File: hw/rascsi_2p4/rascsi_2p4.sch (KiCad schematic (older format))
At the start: 89 parts, among them J1 Raspberry_Pi_2_3, J2 DNP, J4 I2C Pinout, J5 DNP, J6 CONNFLY DB-25, J7 DNP, U1 74ALVC164245DGG, U2 74ALVC164245DGG, U3 UCC5606PWPTR, U4 UCC5606PWPTR, X1 Mac, X3 Mac, X7 Pi, X8 Pi

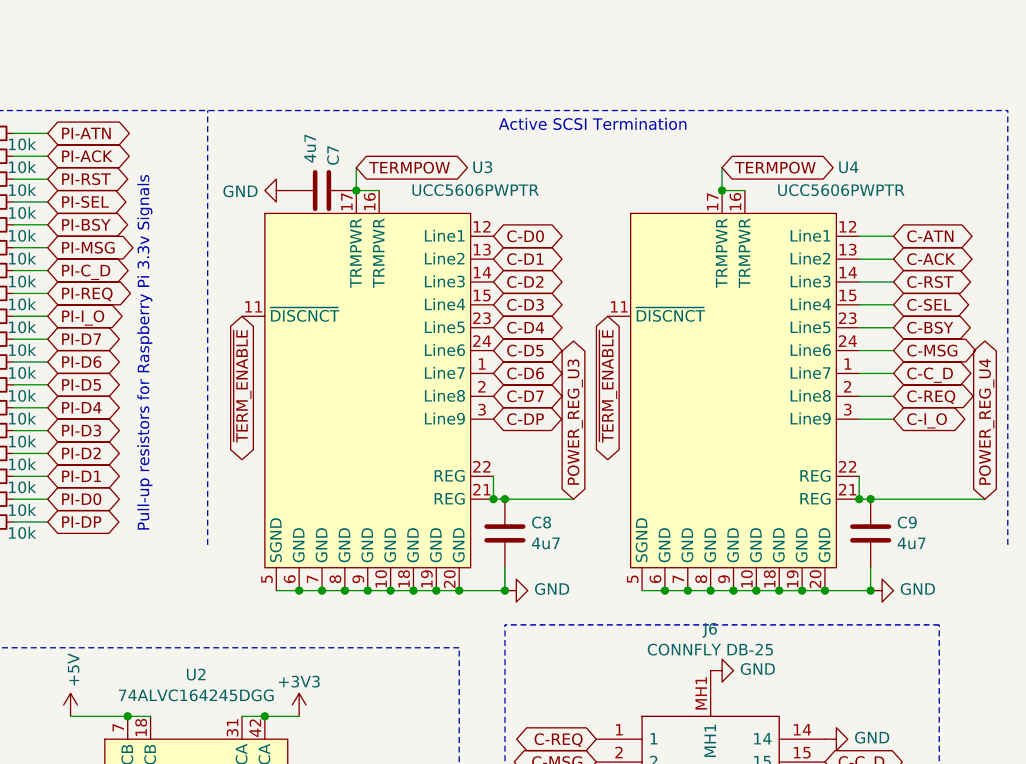
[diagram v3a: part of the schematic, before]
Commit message: moved C9 and C8 for successful routing
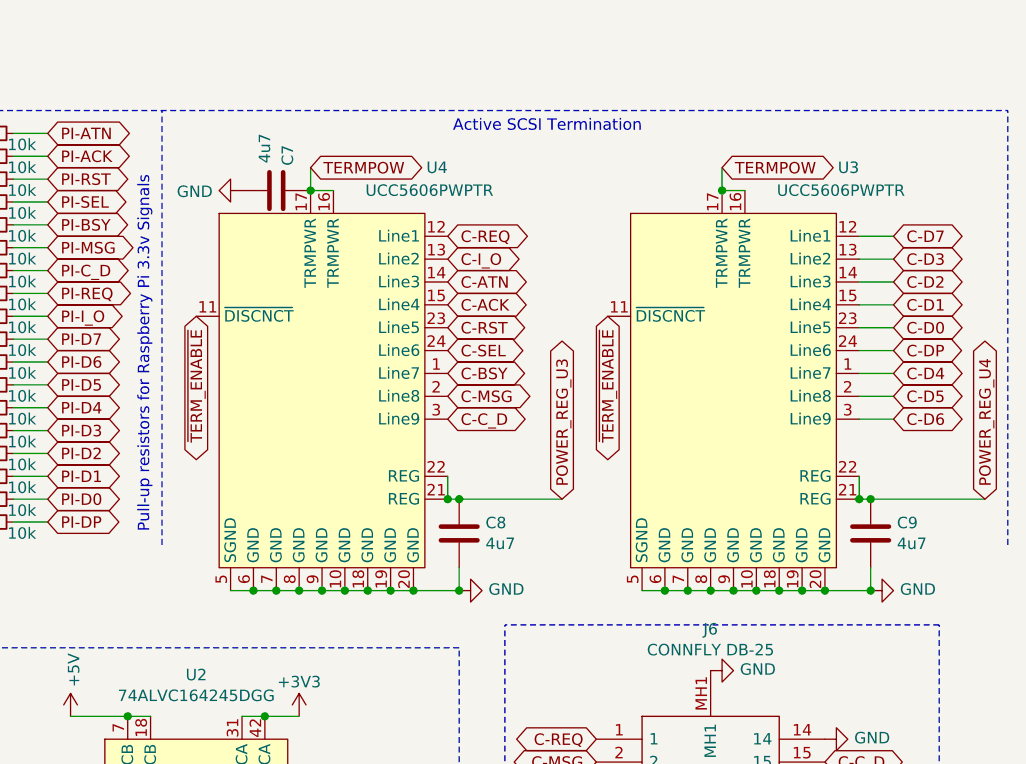
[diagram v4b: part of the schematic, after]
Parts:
- renumbered U4 to U3, U3 to U4
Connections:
- net C-ACK: now also U4.15 (Line4); no longer U3.13 (Line2)
- net C-ATN: now also U4.14 (Line3); no longer U3.12 (Line1)
- net C-BSY: now also U4.1 (Line7); no longer U3.23 (Line5)
- net C-C_D: now also U4.3 (Line9); no longer U3.1 (Line7)
- net C-D0: now also U3.23 (Line5); no longer U4.12 (Line1)
- net C-D1: now also U3.15 (Line4); no longer U4.13 (Line2)
- net C-D2: now also U3.14 (Line3); no longer U4.14 (Line3)
- net C-D3: now also U3.13 (Line2); no longer U4.15 (Line4)
- net C-D4: now also U3.1 (Line7); no longer U4.23 (Line5)
- net C-D5: now also U3.2 (Line8); no longer U4.24 (Line6)
- net C-D6: now also U3.3 (Line9); no longer U4.1 (Line7)
- net C-D7: now also U3.12 (Line1); no longer U4.2 (Line8)
- net C-DP: now also U3.24 (Line6); no longer U4.3 (Line9)
- net C-I_O: now also U4.13 (Line2); no longer U3.3 (Line9)
- net C-MSG: now also U4.2 (Line8); no longer U3.24 (Line6)
- net C-REQ: now also U4.12 (Line1); no longer U3.2 (Line8)
- net C-RST: now also U4.23 (Line5); no longer U3.14 (Line3)
- net C-SEL: now also U4.24 (Line6); no longer U3.15 (Line4)
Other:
- moved on the sheet: C7, C8, U4
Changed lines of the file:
@@
 Text Notes 5300 6300 0    59   Italic 0
 Note the original RaSCSI design calls the DIR pin "ATOB"\nEnable Input ("G") is active low, so always grounded.
-Text GLabel 10000 1900 2    50   BiDi ~ 0
+Text GLabel 8050 1200 2    50   BiDi ~ 0
 C-I_O
 $Comp
@@
 Wire Wire Line
 	5800 2150 5800 2250
-Text GLabel 10000 1400 2    50   BiDi ~ 0
+Text GLabel 8050 1600 2    50   BiDi ~ 0
 C-SEL
-Text GLabel 10000 1300 2    50   BiDi ~ 0
+Text GLabel 8050 1500 2    50   BiDi ~ 0
 C-RST
-Text GLabel 10000 1200 2    50   BiDi ~ 0
+Text GLabel 8050 1400 2    50   BiDi ~ 0
 C-ACK
-Text GLabel 10000 1100 2    50   BiDi ~ 0
+Text GLabel 8050 1300 2    50   BiDi ~ 0
 C-ATN
-Text GLabel 10000 1800 2    50   BiDi ~ 0
+Text GLabel 8050 1100 2    50   BiDi ~ 0
 C-REQ
-Text GLabel 10000 1700 2    50   BiDi ~ 0
+Text GLabel 8050 1900 2    50   BiDi ~ 0
 C-C_D
-Text GLabel 10000 1600 2    50   BiDi ~ 0
+Text GLabel 8050 1800 2    50   BiDi ~ 0
 C-MSG
-Text GLabel 10000 1500 2    50   BiDi ~ 0
+Text GLabel 8050 1700 2    50   BiDi ~ 0
 C-BSY
-Text GLabel 8250 1900 2    50   BiDi ~ 0
+Text GLabel 10000 1600 2    50   BiDi ~ 0
 C-DP
-Text GLabel 8250 1800 2    50   BiDi ~ 0
+Text GLabel 10000 1100 2    50   BiDi ~ 0
 C-D7
-Text GLabel 8250 1700 2    50   BiDi ~ 0
+Text GLabel 10000 1900 2    50   BiDi ~ 0
 C-D6
-Text GLabel 8250 1600 2    50   BiDi ~ 0
+Text GLabel 10000 1800 2    50   BiDi ~ 0
 C-D5
-Text GLabel 8250 1500 2    50   BiDi ~ 0
+Text GLabel 10000 1700 2    50   BiDi ~ 0
 C-D4
-Text GLabel 8250 1400 2    50   BiDi ~ 0
+Text GLabel 10000 1200 2    50   BiDi ~ 0
 C-D3
-Text GLabel 8250 1300 2    50   BiDi ~ 0
+Text GLabel 10000 1300 2    50   BiDi ~ 0
 C-D2
-Text GLabel 8250 1200 2    50   BiDi ~ 0
+Text GLabel 10000 1400 2    50   BiDi ~ 0
 C-D1
-Text GLabel 8250 1100 2    50   BiDi ~ 0
+Text GLabel 10000 1500 2    50   BiDi ~ 0
 C-D0
 Wire Wire Line
@@
 	5450 2450 5450 550
 Wire Notes Line
-	7000 2450 7000 550
+	6800 2450 6800 550
 Wire Notes Line
 	2900 2450 5300 2450
@@
 Connection ~ 1150 7050
 $Comp
-L amiga:UCC5606PWPTR U3
+L amiga:UCC5606PWPTR U4
 U 1 1 628EED4A
-P 7700 1750
-F 0 "U3" H 8250 2700 50  0000 R CNN
-F 1 "UCC5606PWPTR" H 8450 2600 50  0000 R CNN
-F 2 "Package_SO:TSSOP-24_6.1x7.8mm_P0.65mm" H 7700 400 50  0001 C CNN
-F 3 "http://www.ti.com/general/docs/suppproductinfo.tsp?distId=26&gotoUrl=http%3A%2F%2Fwww.ti.com%2Flitv%2Fslus347a" H 8000 950 50  0001 C CNN
-	1    7700 1750
+P 7500 1750
+F 0 "U4" H 8050 2700 50  0000 R CNN
+F 1 "UCC5606PWPTR" H 8250 2600 50  0000 R CNN
+F 2 "Package_SO:TSSOP-24_6.1x7.8mm_P0.65mm" H 7500 400 50  0001 C CNN
+F 3 "http://www.ti.com/general/docs/suppproductinfo.tsp?distId=26&gotoUrl=http%3A%2F%2Fwww.ti.com%2Flitv%2Fslus347a" H 7800 950 50  0001 C CNN
+	1    7500 1750
 	1    0    0    -1
 $EndComp
@@
 L Device:C C8
 U 1 1 628F5101
-P 8300 2400
-F 0 "C8" H 8415 2446 50  0000 L CNN
-F 1 "4u7" H 8415 2355 50  0000 L CNN
-F 2 "Capacitor_SMD:C_0805_2012Metric" H 8338 2250 50  0001 C CNN
-F 3 "https://datasheet.lcsc.com/szlcsc/Samsung-Electro-Mechanics-CL21A475KAQNNNE_C1779.pdf" H 8300 2400 50  0001 C CNN
-F 4 "C1779" H 8300 2400 50  0001 C CNN "LCSC"
-F 5 "Samsung Electro-Mechanics" H 8300 2400 50  0001 C CNN "Manufacturer_Name"
-F 6 "CL21A475KAQNNNE" H 8300 2400 50  0001 C CNN "Manufacturer_Part_Number"
-	1    8300 2400
+P 8100 2400
+F 0 "C8" H 8215 2446 50  0000 L CNN
+F 1 "4u7" H 8215 2355 50  0000 L CNN
+F 2 "Capacitor_SMD:C_0805_2012Metric" H 8138 2250 50  0001 C CNN
+F 3 "https://datasheet.lcsc.com/szlcsc/Samsung-Electro-Mechanics-CL21A475KAQNNNE_C1779.pdf" H 8100 2400 50  0001 C CNN
+F 4 "C1779" H 8100 2400 50  0001 C CNN "LCSC"
+F 5 "Samsung Electro-Mechanics" H 8100 2400 50  0001 C CNN "Manufacturer_Name"
+F 6 "CL21A475KAQNNNE" H 8100 2400 50  0001 C CNN "Manufacturer_Part_Number"
+	1    8100 2400
 	1    0    0    -1
 $EndComp
 Wire Wire Line
-	8250 2150 8250 2250
+	8050 2150 8050 2250
 Wire Wire Line
-	8250 2250 8300 2250
-Connection ~ 8250 2250
+	8050 2250 8100 2250
+Connection ~ 8050 2250
 $Comp
 L power:GND #PWR0109
 U 1 1 629679DA
-P 8300 2650
-F 0 "#PWR0109" H 8300 2400 50  0001 C CNN
-F 1 "GND" V 8305 2522 50  0000 R CNN
-F 2 "" H 8300 2650 50  0001 C CNN
-F 3 "" H 8300 2650 50  0001 C CNN
-	1    8300 2650
+P 8100 2650
+F 0 "#PWR0109" H 8100 2400 50  0001 C CNN
+F 1 "GND" V 8105 2522 50  0000 R CNN
+F 2 "" H 8100 2650 50  0001 C CNN
+F 3 "" H 8100 2650 50  0001 C CNN
+	1    8100 2650
 	0    -1   -1   0
 $EndComp
 Wire Wire Line
+	7100 2650 7200 2650
+Connection ~ 7200 2650
+Wire Wire Line
+	7200 2650 7300 2650
+Wire Wire Line
 	7300 2650 7400 2650
-Connection ~ 7400 2650
+Connection ~ 7300 2650
 Wire Wire Line
 	7400 2650 7500 2650
+Connection ~ 7400 2650
 Wire Wire Line
 	7500 2650 7600 2650
@@
 Connection ~ 7800 2650
 Wire Wire Line
-	7900 2650 8000 2650
-Connection ~ 7900 2650
-Wire Wire Line
-	8000 2650 8100 2650
-Connection ~ 8000 2650
+	7900 2650 8100 2650
 Wire Wire Line
-	8100 2650 8300 2650
-Wire Wire Line
-	8300 2650 8300 2550
-Connection ~ 8100 2650
+	8100 2650 8100 2550
+Connection ~ 7900 2650
 Wire Wire Line
-	7650 900  7750 900
-Connection ~ 7650 900
+	7450 900  7550 900
+Connection ~ 7450 900
 $Comp
 L Device:C C7
 U 1 1 62AF0127
-P 7500 900
-F 0 "C7" H 7300 950 50  0000 L CNN
-F 1 "4u7" H 7250 850 50  0000 L CNN
-F 2 "Capacitor_SMD:C_0805_2012Metric" H 7538 750 50  0001 C CNN
-F 3 "https://datasheet.lcsc.com/szlcsc/Samsung-Electro-Mechanics-CL21A475KAQNNNE_C1779.pdf" H 7500 900 50  0001 C CNN
-F 4 "C1779" H 7500 900 50  0001 C CNN "LCSC"
-F 5 "Samsung Electro-Mechanics" H 7500 900 50  0001 C CNN "Manufacturer_Name"
-F 6 "CL21A475KAQNNNE" H 7500 900 50  0001 C CNN "Manufacturer_Part_Number"
-	1    7500 900
+P 7300 900
+F 0 "C7" H 7100 950 50  0000 L CNN
+F 1 "4u7" H 7050 850 50  0000 L CNN
+F 2 "Capacitor_SMD:C_0805_2012Metric" H 7338 750 50  0001 C CNN
+F 3 "https://datasheet.lcsc.com/szlcsc/Samsung-Electro-Mechanics-CL21A475KAQNNNE_C1779.pdf" H 7300 900 50  0001 C CNN
+F 4 "C1779" H 7300 900 50  0001 C CNN "LCSC"
+F 5 "Samsung Electro-Mechanics" H 7300 900 50  0001 C CNN "Manufacturer_Name"
+F 6 "CL21A475KAQNNNE" H 7300 900 50  0001 C CNN "Manufacturer_Part_Number"
+	1    7300 900
 	0    1    1    0
 $EndComp
@@
 L power:GND #PWR0110
 U 1 1 62AF169D
-P 7350 900
-F 0 "#PWR0110" H 7350 650 50  0001 C CNN
-F 1 "GND" V 7355 772 50  0000 R CNN
-F 2 "" H 7350 900 50  0001 C CNN
-F 3 "" H 7350 900 50  0001 C CNN
-	1    7350 900
+P 7150 900
+F 0 "#PWR0110" H 7150 650 50  0001 C CNN
+F 1 "GND" V 7155 772 50  0000 R CNN
+F 2 "" H 7150 900 50  0001 C CNN
+F 3 "" H 7150 900 50  0001 C CNN
+	1    7150 900
 	0    1    1    0
 $EndComp
@@
 Wire Wire Line
 	1200 1400 1200 1450
-Text GLabel 7150 1450 3    50   BiDi ~ 0
+Text GLabel 6950 1450 3    50   BiDi ~ 0
 ~TERM_ENABLE
 $Comp
-L amiga:UCC5606PWPTR U4
+L amiga:UCC5606PWPTR U3
 U 1 1 62E764ED
 P 9300 1750
-F 0 "U4" H 9850 2700 50  0000 R CNN
+F 0 "U3" H 9850 2700 50  0000 R CNN
 F 1 "UCC5606PWPTR" H 10050 2600 50  0000 R CNN
 F 2 "Package_SO:TSSOP-24_6.1x7.8mm_P0.65mm" H 9300 400 50  0001 C CNN
@@
 Text GLabel 8750 1450 3    50   BiDi ~ 0
 ~TERM_ENABLE
-Text Notes 9100 650  2    50   ~ 0
+Text Notes 8900 650  2    50   ~ 0
 Active SCSI Termination
-Connection ~ 8300 2650
+Connection ~ 8100 2650
 Connection ~ 9900 2650
-Text GLabel 7650 800  2    50   BiDi ~ 0
+Text GLabel 7450 800  2    50   BiDi ~ 0
 TERMPOW
 Wire Wire Line
-	7650 800  7650 900
+	7450 800  7450 900
 Text GLabel 9250 800  2    50   BiDi ~ 0
 TERMPOW
@@
 	3750 1600 3750 1500
 Connection ~ 3750 1500
-Text GLabel 8600 2250 1    50   BiDi ~ 0
+Text GLabel 8550 2250 1    50   BiDi ~ 0
 POWER_REG_U3
 Text GLabel 10400 2250 1    50   BiDi ~ 0
 POWER_REG_U4
 Wire Wire Line
-	8600 2250 8300 2250
-Connection ~ 8300 2250
+	8550 2250 8100 2250
+Connection ~ 8100 2250
 Wire Wire Line
 	10400 2250 9900 2250

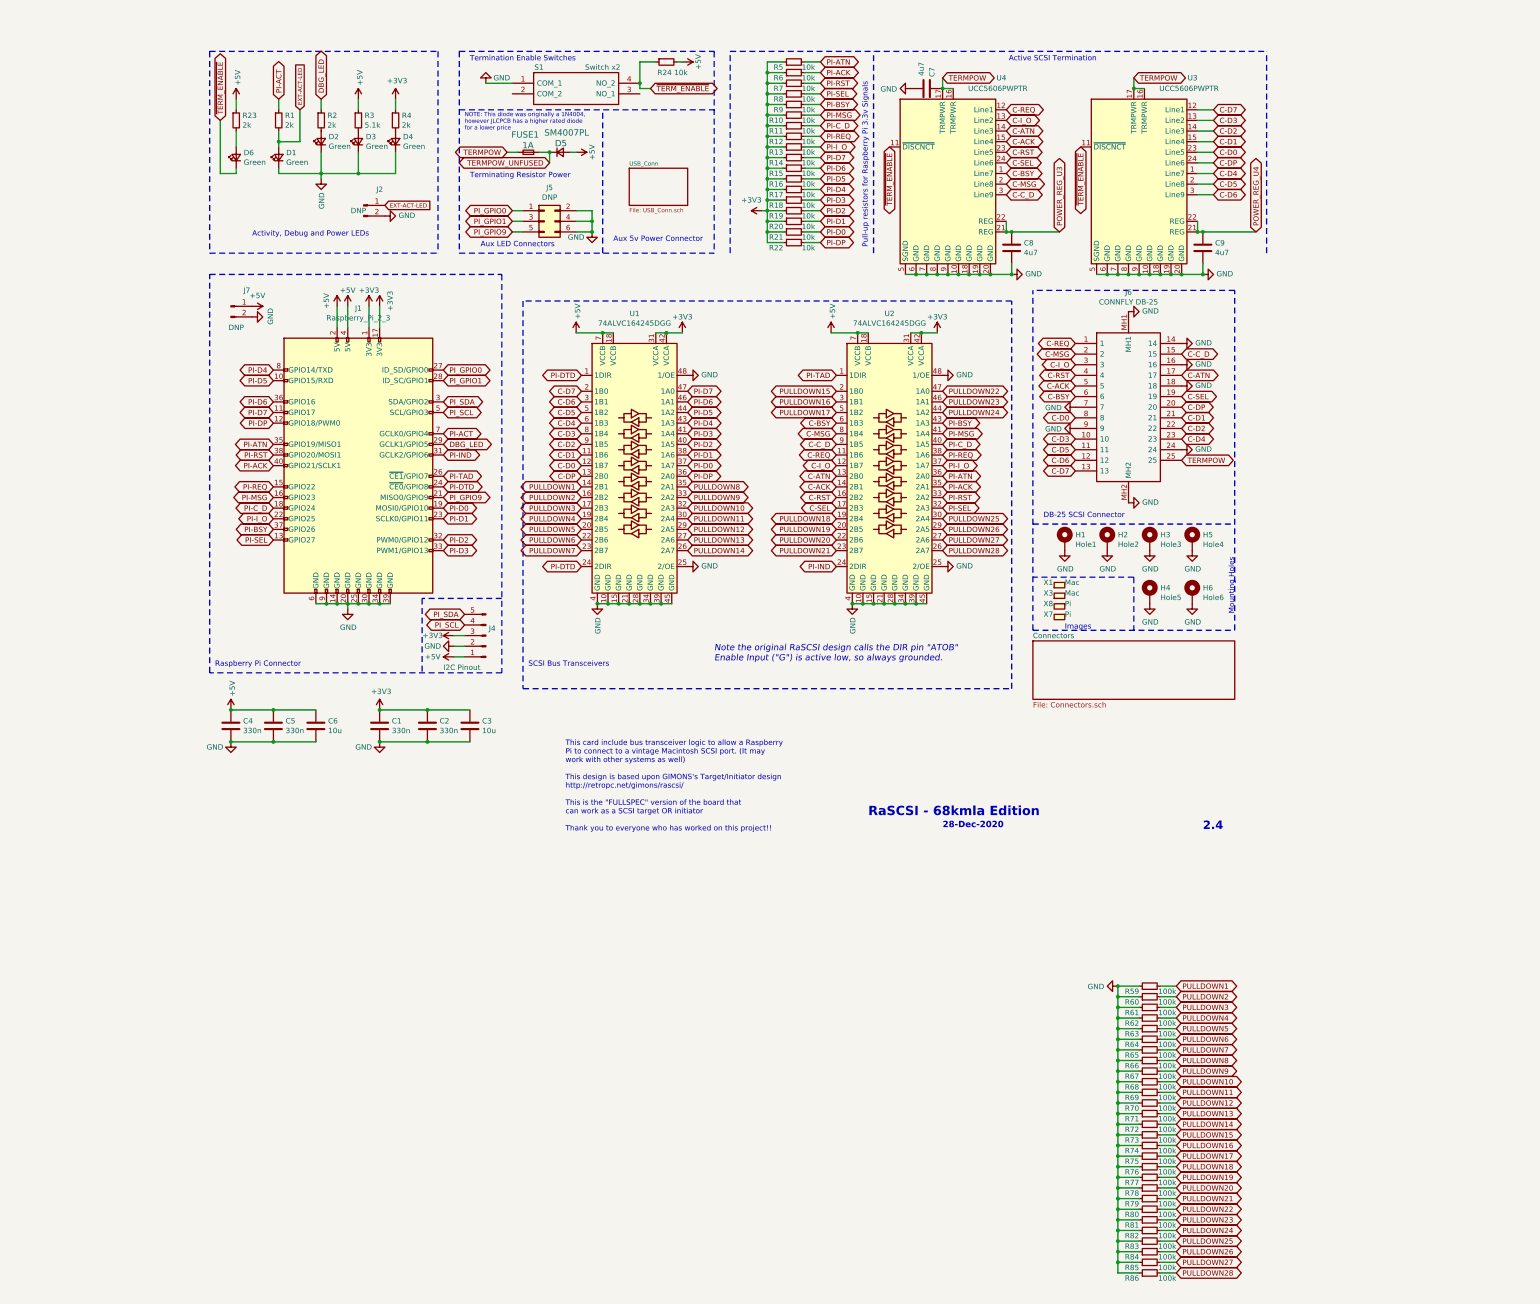
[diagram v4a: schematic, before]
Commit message: added NarrowPowerAdapter to easy routing
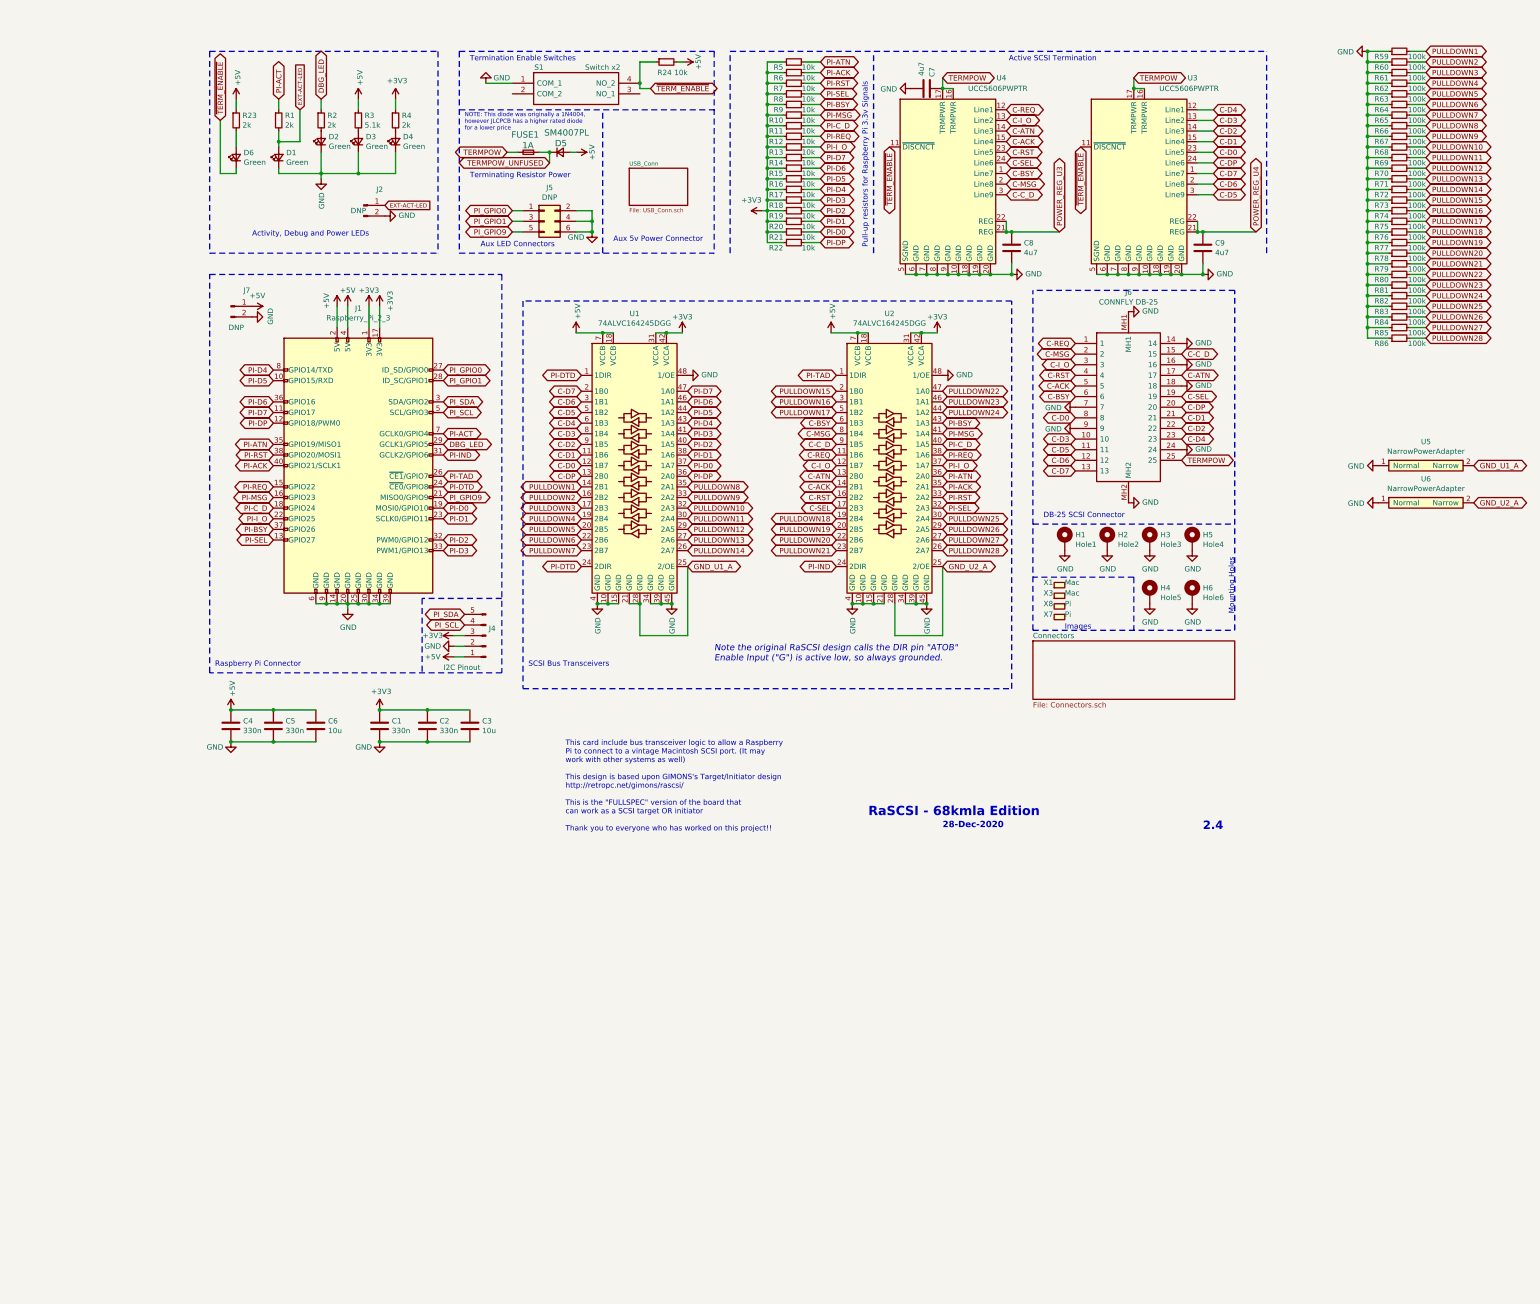
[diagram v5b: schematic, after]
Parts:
- added U5, U6: NarrowPowerAdapter, amiga:NarrowPowerAdapter_0.60_to_0.25, symbol amiga:NarrowPowerAdapter
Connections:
- net C-D4: now also U3.12 (Line1); no longer U3.1 (Line7)
- net C-D5: now also U3.3 (Line9); no longer U3.2 (Line8)
- net C-D6: now also U3.2 (Line8); no longer U3.3 (Line9)
- net C-D7: now also U3.1 (Line7); no longer U3.12 (Line1)
- net GND: now also U5.1 (Normal), U6.1 (Normal); no longer U1.21 (GND), U1.25 (2/OE), U1.28 (GND), U2.25 (2/OE), U2.28 (GND)
- new net GND_U1_A: U1.21 (GND), U1.25 (2/OE), U1.28 (GND), U5.2 (Narrow)
- new net GND_U2_A: U2.25 (2/OE), U2.28 (GND), U6.2 (Narrow)
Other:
- moved on the sheet: R59, R60, R61, R62, R63, R64, R65, R66, R67, R68, R69, R70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
